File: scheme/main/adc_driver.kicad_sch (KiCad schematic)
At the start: 2 parts

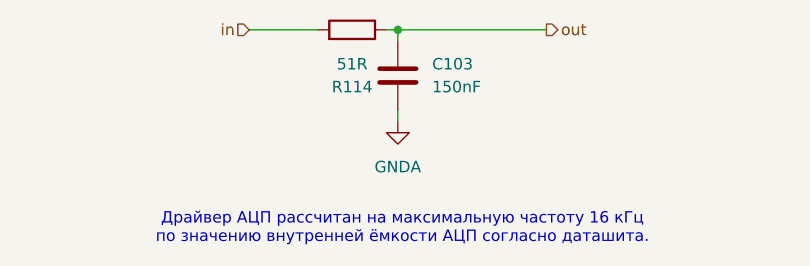
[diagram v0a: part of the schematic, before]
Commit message: added input buffer
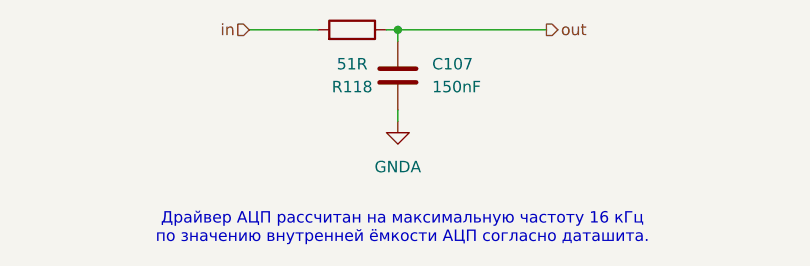
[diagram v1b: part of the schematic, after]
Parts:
- renumbered C103 to C107, R114 to R118
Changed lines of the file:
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@@
 		(on_board yes)
 		(dnp no)
-		(property "Reference" "R114"
+		(property "Reference" "R118"
 			(at 73.66 62.23 90)
 			(effects
@@
 		(on_board yes)
 		(dnp no)
-		(property "Reference" "C103"
+		(property "Reference" "C107"
 			(at 82.55 59.6899 0)
 			(effects
@@
 		(dnp no)
 		(fields_autoplaced yes)
-		(property "Reference" "#PWR131"
+		(property "Reference" "#PWR136"
 			(at 78.74 72.39 0)
 			(effects

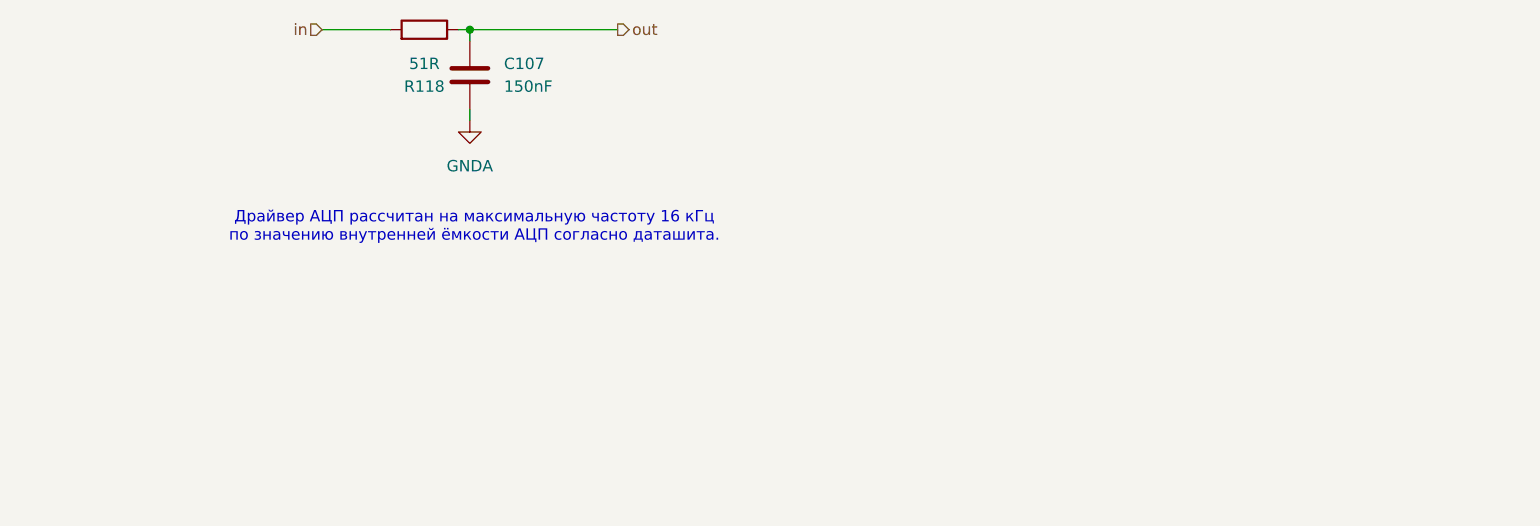
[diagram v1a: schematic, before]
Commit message: added 24V & GND to DO terminal & more
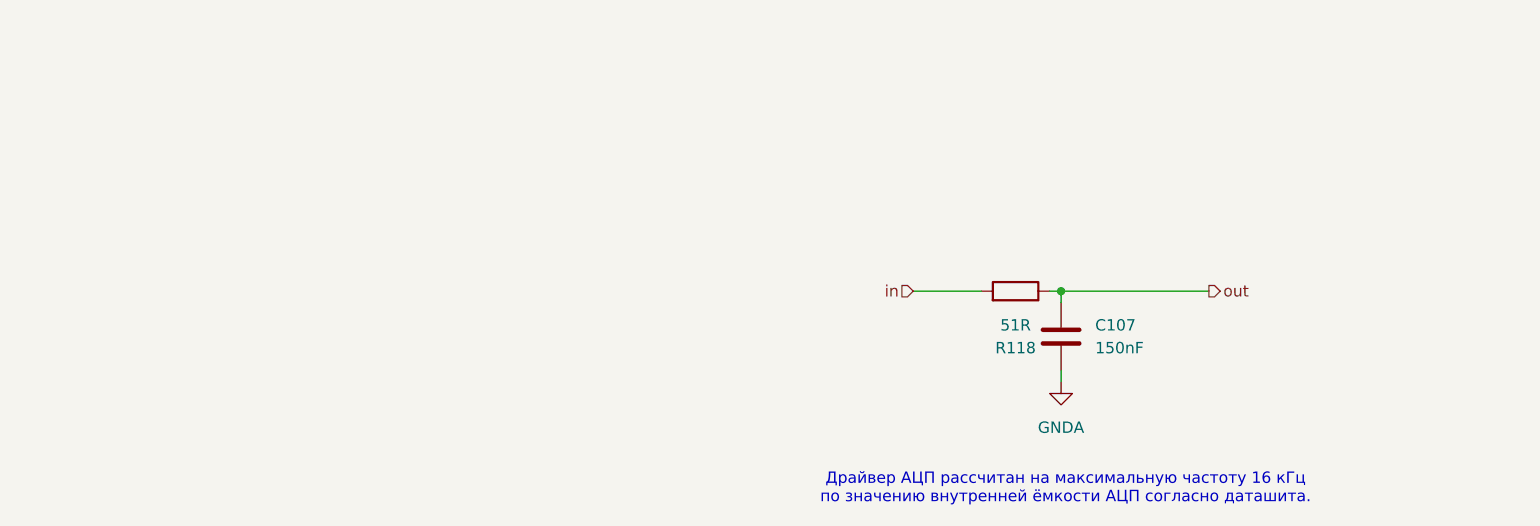
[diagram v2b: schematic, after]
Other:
- moved on the sheet: C107, R118
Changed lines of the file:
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@@
 	(paper "A4")
 	(junction
-		(at 78.74 55.88)
+		(at 144.78 85.09)
 		(diameter 0)
 		(color 0 0 0 0)
@@
 	(wire
 		(pts
-			(xy 77.47 55.88) (xy 78.74 55.88)
-		)
-		(stroke
-			(width 0)
-			(type default)
-		)
-	)
-	(wire
-		(pts
-			(xy 62.23 55.88) (xy 69.85 55.88)
-		)
-		(stroke
-			(width 0)
-			(type default)
-		)
-	)
-	(wire
-		(pts
-			(xy 78.74 55.88) (xy 95.25 55.88)
-		)
-		(stroke
-			(width 0)
-			(type default)
-		)
-	)
-	(wire
-		(pts
-			(xy 78.74 55.88) (xy 78.74 57.15)
-		)
-		(stroke
-			(width 0)
-			(type default)
-		)
-	)
-	(wire
-		(pts
-			(xy 78.74 64.77) (xy 78.74 66.04)
+			(xy 143.51 85.09) (xy 144.78 85.09)
+		)
+		(stroke
+			(width 0)
+			(type default)
+		)
+	)
+	(wire
+		(pts
+			(xy 128.27 85.09) (xy 135.89 85.09)
+		)
+		(stroke
+			(width 0)
+			(type default)
+		)
+	)
+	(wire
+		(pts
+			(xy 144.78 85.09) (xy 161.29 85.09)
+		)
+		(stroke
+			(width 0)
+			(type default)
+		)
+	)
+	(wire
+		(pts
+			(xy 144.78 85.09) (xy 144.78 86.36)
+		)
+		(stroke
+			(width 0)
+			(type default)
+		)
+	)
+	(wire
+		(pts
+			(xy 144.78 93.98) (xy 144.78 95.25)
 		)
 		(stroke
@@
 	(text "Драйвер АЦП рассчитан на максимальную частоту 16 кГц\nпо значению внутренней ёмкости АЦП согласно даташита."
 		(exclude_from_sim no)
-		(at 79.248 77.978 0)
+		(at 145.288 107.188 0)
 		(effects
 			(font
@@
 	(hierarchical_label "in"
 		(shape input)
-		(at 62.23 55.88 180)
+		(at 128.27 85.09 180)
 		(effects
 			(font
@@
 	(hierarchical_label "out"
 		(shape output)
-		(at 95.25 55.88 0)
+		(at 161.29 85.09 0)
 		(effects
 			(font
@@
 	(symbol
 		(lib_id "Device:R")
-		(at 73.66 55.88 270)
+		(at 139.7 85.09 270)
 		(mirror x)
 		(unit 1)
@@
 		(dnp no)
 		(property "Reference" "R118"
-			(at 73.66 62.23 90)
+			(at 139.7 91.44 90)
 			(effects
 				(font
@@
 		)
 		(property "Value" "51R"
-			(at 73.66 59.69 90)
+			(at 139.7 88.9 90)
 			(effects
 				(font
@@
 		)
 		(property "Footprint" "Resistor_SMD:R_0805_2012Metric"
-			(at 73.66 57.658 90)
+			(at 139.7 86.868 90)
 			(effects
 				(font
@@
 		)
 		(property "Datasheet" "~"
-			(at 73.66 55.88 0)
+			(at 139.7 85.09 0)
 			(effects
 				(font
@@
 		)
 		(property "Description" "Resistor"
-			(at 73.66 55.88 0)
+			(at 139.7 85.09 0)
 			(effects
 				(font
@@
 	(symbol
 		(lib_id "Device:C")
-		(at 78.74 60.96 180)
+		(at 144.78 90.17 180)
 		(unit 1)
 		(exclude_from_sim no)
@@
 		(dnp no)
 		(property "Reference" "C107"
-			(at 82.55 59.6899 0)
+			(at 148.59 88.8999 0)
 			(effects
 				(font
@@
 		)
 		(property "Value" "150nF"
-			(at 82.55 62.2299 0)
+			(at 148.59 91.4399 0)
 			(effects
 				(font
@@
 		)
 		(property "Footprint" "Capacitor_SMD:C_0805_2012Metric"
-			(at 77.7748 57.15 0)
+			(at 143.8148 86.36 0)
 			(effects
 				(font
@@
 		)
 		(property "Datasheet" "~"
-			(at 78.74 60.96 0)
+			(at 144.78 90.17 0)
 			(effects
 				(font
@@
 		)
 		(property "Description" "Unpolarized capacitor"
-			(at 78.74 60.96 0)
+			(at 144.78 90.17 0)
 			(effects
 				(font
@@
 	(symbol
 		(lib_id "power:GNDA")
-		(at 78.74 66.04 0)
+		(at 144.78 95.25 0)
 		(unit 1)
 		(exclude_from_sim no)
@@
 		(fields_autoplaced yes)
 		(property "Reference" "#PWR136"
-			(at 78.74 72.39 0)
+			(at 144.78 101.6 0)
 			(effects
 				(font
@@
 		)
 		(property "Value" "GNDA"
-			(at 78.74 71.12 0)
+			(at 144.78 100.33 0)
 			(effects
 				(font
@@
 		)
 		(property "Footprint" ""
-			(at 78.74 66.04 0)
+			(at 144.78 95.25 0)
 			(effects
 				(font
@@
 		)
 		(property "Datasheet" ""
-			(at 78.74 66.04 0)
+			(at 144.78 95.25 0)
 			(effects
 				(font
@@
 		)
 		(property "Description" "Power symbol creates a global label with name \"GNDA\" , analog ground"
-			(at 78.74 66.04 0)
-			(effects
-				(font
+			(at 144.78 95.25 0)
+			(effects
+				(font

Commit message: sheets titles
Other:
- title: (none) -> Драйвер АЦП
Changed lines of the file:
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@@
 	(generator_version "8.0")
 	(paper "A4")
+	(title_block
+		(title "Драйвер АЦП")
+	)
 	(junction
 		(at 144.78 85.09)
